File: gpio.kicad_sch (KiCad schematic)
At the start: 5 parts, among them J1 CONN_02X20, J2 CONN_02X20, U1 LFE5U-85F-6BG381C

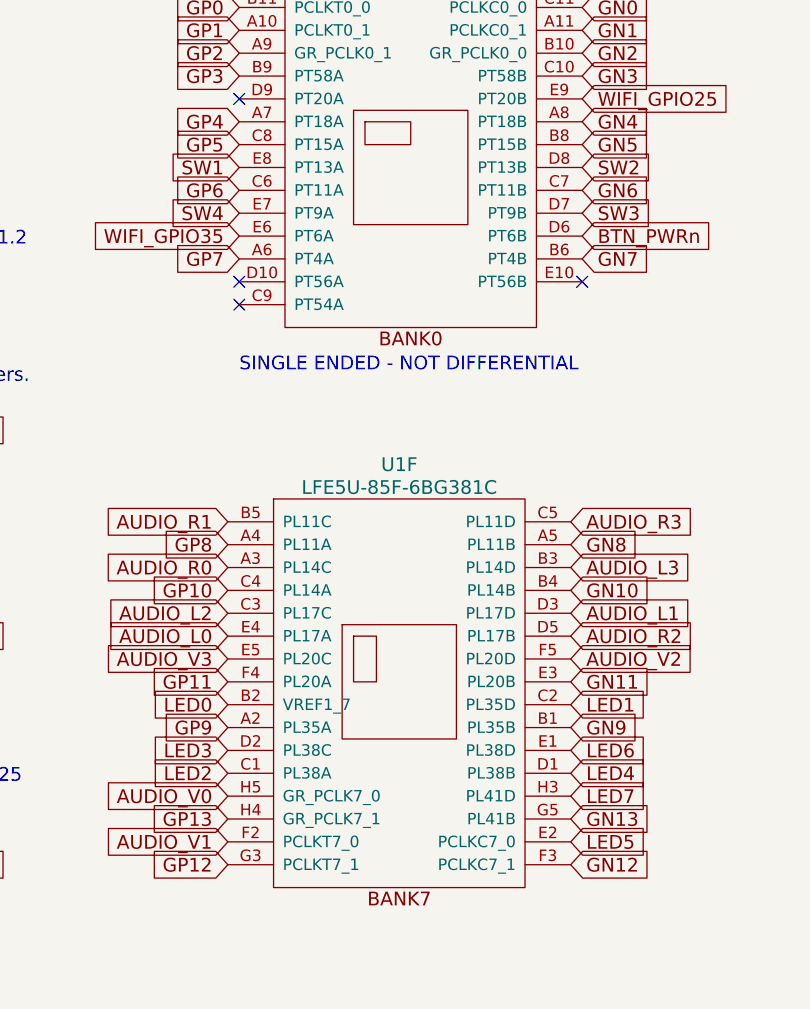
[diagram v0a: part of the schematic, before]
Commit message: remove unneeded components from schema
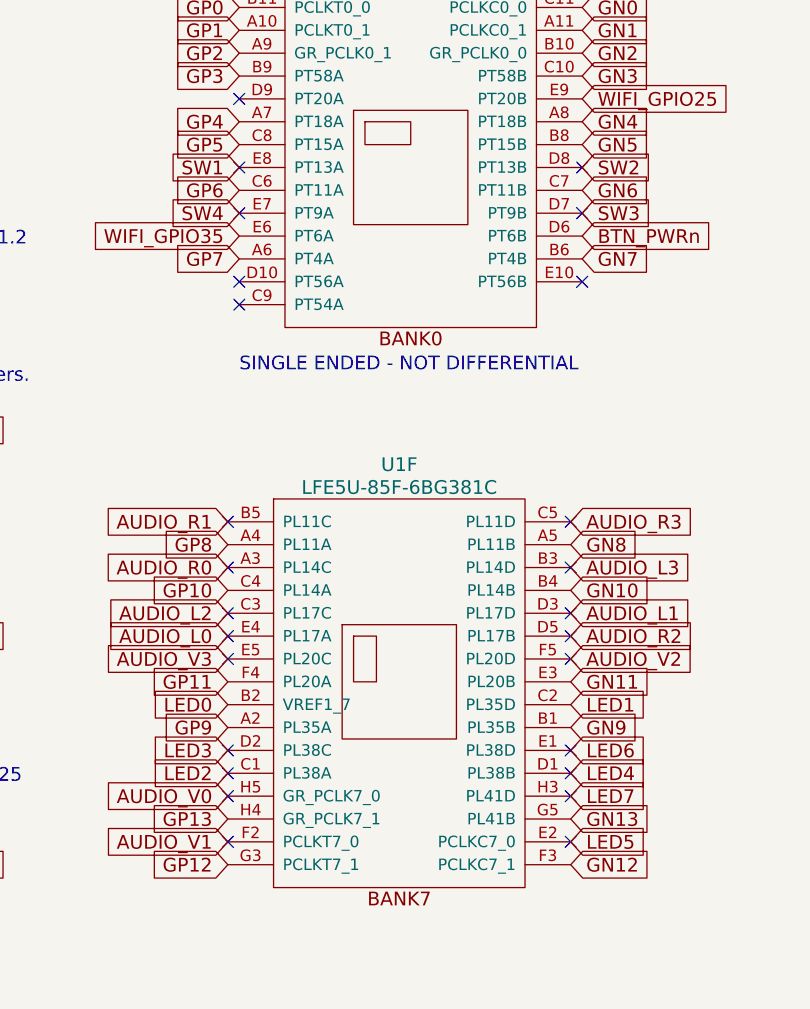
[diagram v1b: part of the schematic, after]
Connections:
- no-connect marks 4 -> 26
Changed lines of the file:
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@@
+	)
+	(no_connect
+		(at 143.51 130.81)
+	)
+	(no_connect
+		(at 105.41 102.87)
+	)
+	(no_connect
+		(at 143.51 113.03)
+	)
+	(no_connect
+		(at 105.41 113.03)
+	)
+	(no_connect
+		(at 105.41 133.35)
 	)
 	(no_connect
@@
 	)
 	(no_connect
+		(at 105.41 138.43)
+	)
+	(no_connect
+		(at 143.51 118.11)
+	)
+	(no_connect
+		(at 105.41 130.81)
+	)
+	(no_connect
+		(at 144.78 63.5)
+	)
+	(no_connect
+		(at 105.41 118.11)
+	)
+	(no_connect
+		(at 106.68 63.5)
+	)
+	(no_connect
+		(at 143.51 115.57)
+	)
+	(no_connect
+		(at 106.68 68.58)
+	)
+	(no_connect
+		(at 143.51 138.43)
+	)
+	(no_connect
+		(at 143.51 133.35)
+	)
+	(no_connect
+		(at 105.41 115.57)
+	)
+	(no_connect
 		(at 106.68 78.74)
+	)
+	(no_connect
+		(at 105.41 128.27)
+	)
+	(no_connect
+		(at 143.51 102.87)
+	)
+	(no_connect
+		(at 144.78 68.58)
+	)
+	(no_connect
+		(at 105.41 107.95)
+	)
+	(no_connect
+		(at 143.51 107.95)
 	)
 	(no_connect
@@
 	)
 	(no_connect
+		(at 143.51 128.27)
+	)
+	(no_connect

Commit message: start to normalize bom
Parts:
- D51, D52, J1, J2: now left out of the parts list
- U1: Digikey (none) -> 220-2177-ND; LCSC (none) -> C446029
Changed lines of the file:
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@@
 		(unit 1)
 		(exclude_from_sim no)
-		(in_bom yes)
+		(in_bom no)
 		(on_board yes)
 		(dnp no)
@@
 		(unit 1)
 		(exclude_from_sim no)
-		(in_bom yes)
+		(in_bom no)
 		(on_board yes)
 		(dnp no)
@@
 		(unit 1)
 		(exclude_from_sim no)
-		(in_bom yes)
+		(in_bom no)
 		(on_board yes)
 		(dnp no)
@@
 		(unit 1)
 		(exclude_from_sim no)
-		(in_bom yes)
+		(in_bom no)
 		(on_board yes)
 		(dnp no)
@@
 			)
 		)
+		(property "LCSC" "C446029"
+			(at 125.73 63.5 0)
+			(effects
+				(font
+					(size 1.27 1.27)
+				)
+				(hide yes)
+			)
+		)
+		(property "Digikey" "220-2177-ND"
+			(at 125.73 63.5 0)
+			(effects
+				(font
+					(size 1.27 1.27)
+				)
+				(hide yes)
+			)
+		)
 		(pin "B11"
 		)
@@
 				)
 				(hide yes)
+			)
+		)
+		(property "LCSC" "C446029"
+			(at 124.46 120.65 0)
+			(effects
+				(font
+					(size 1.27 1.27)
+				)
+				(hide yes)
+			)
+		)
+		(property "Digikey" "220-2177-ND"
+			(at 124.46 120.65 0)
+			(effects
+				(font
+					(size 1.27 1.27)
+				)
+				(hide yes)

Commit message: Remove 'Leave Empty' in favor of using attributes
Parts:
- D51, D52, J1, J2: Note Leave empty -> (none); now not fitted
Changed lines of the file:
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@@
 		(in_bom no)
 		(on_board yes)
-		(in_pos_files yes)
-		(dnp no)
+		(in_pos_files no)
+		(dnp yes)
 		(property "Reference" "D51"
 			(at 189.23 95.25 0)
@@
 			)
 		)
-		(property "Note" "Leave empty"
+		(property "Note" ""
 			(at 189.23 92.71 0)
 			(hide yes)
@@
 		(in_bom no)
 		(on_board yes)
-		(in_pos_files yes)
-		(dnp no)
+		(in_pos_files no)
+		(dnp yes)
 		(property "Reference" "D52"
 			(at 238.76 95.25 0)
@@
 			)
 		)
-		(property "Note" "Leave empty"
+		(property "Note" ""
 			(at 238.76 92.71 0)
 			(hide yes)
@@
 		(in_bom no)
 		(on_board yes)
-		(in_pos_files yes)
-		(dnp no)
+		(in_pos_files no)
+		(dnp yes)
 		(property "Reference" "J2"
 			(at 213.36 143.51 0)
@@
 			)
 		)
-		(property "Note" "Leave empty"
+		(property "Note" ""
 			(at 212.09 118.11 0)
 			(hide yes)
@@
 		(in_bom no)
 		(on_board yes)
-		(in_pos_files yes)
-		(dnp no)
+		(in_pos_files no)
+		(dnp yes)
 		(property "Reference" "J1"
 			(at 48.26 90.17 0)
@@
 			)
 		)
-		(property "Note" "Leave empty"
+		(property "Note" ""
 			(at 49.53 115.57 0)
 			(hide yes)

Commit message: removed optional 2.5 on J1
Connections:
- net 2V5_3V3 is gone; now on net +3V3: J1.1 (Pin_1), J1.19 (Pin_19), J1.2 (Pin_2), J1.20 (Pin_20), J1.39 (Pin_39), J1.40 (Pin_40)

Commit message: remaining thing: i2c connector
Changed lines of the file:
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@@
 			)
 		)
-		(property "Description" ""
+		(property "Description" "ECP5UM85"
 			(at 125.73 63.5 0)
 			(show_name no)

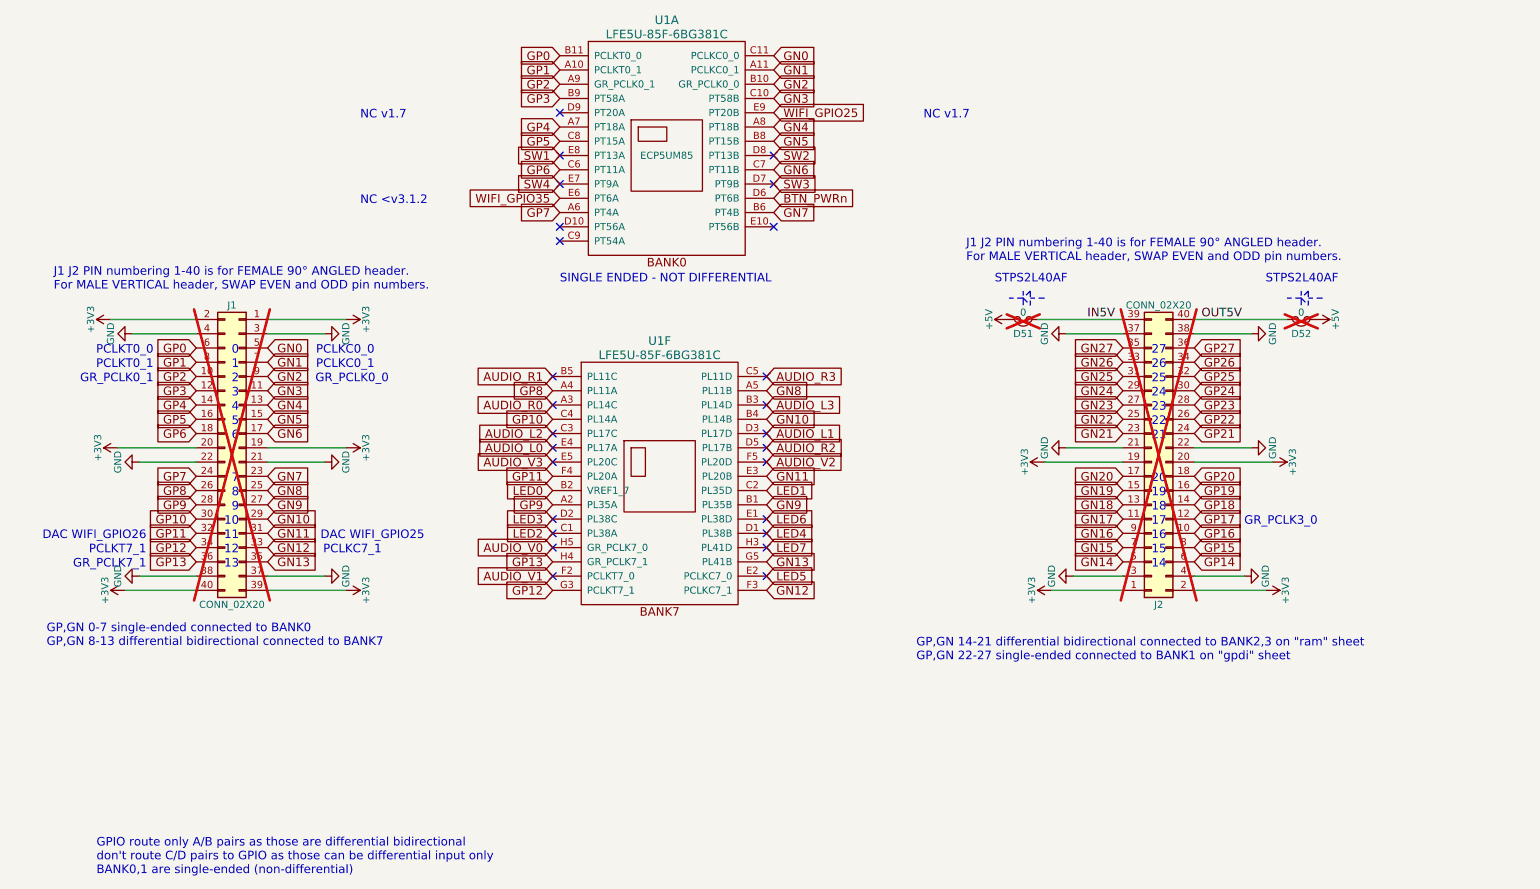
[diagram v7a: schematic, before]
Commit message: reposition flash to bottom. route esp32-s3. fix drc issues
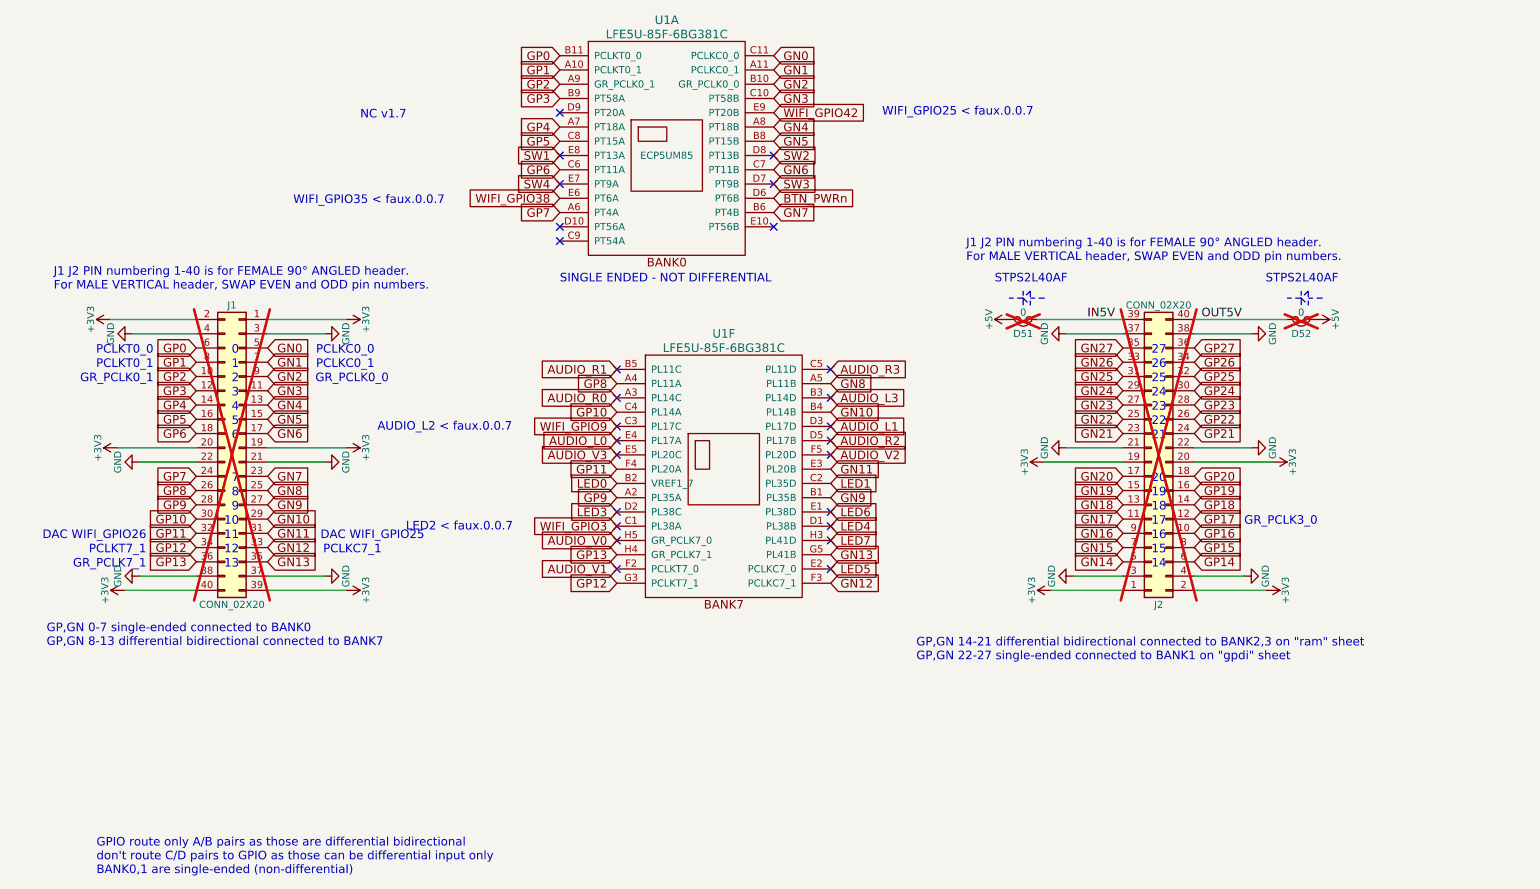
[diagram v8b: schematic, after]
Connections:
- net AUDIO_L2 renamed WIFI_GPIO9
- net LED2 renamed WIFI_GPIO3
- net WIFI_GPIO25 renamed WIFI_GPIO42
- net WIFI_GPIO35 renamed WIFI_GPIO38
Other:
- note added: "AUDIO_L2 < faux.0.0.7"
- note added: "LED2 < faux.0.0.7"
- note added: "WIFI_GPIO25 < faux.0.0.7"
- note added: "WIFI_GPIO35 < faux.0.0.7"
- note removed: "NC <v3.1.2"
- moved on the sheet: U1F
